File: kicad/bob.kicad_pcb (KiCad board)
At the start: 2 copper layers, 58.4 x 25.4 mm, 54 parts, among them J1 Mini USB Female, J2 GPIO (Optional), J3 GPIO (Optional), J4 Battery Connector, J5 Conn_01x03_Male, SW1 Screw Switch, U1 W25Q64JVSS, U2 AMS1117-3.3, U3 RP2040, U4 QMC5883L, U5 QMI8658C, U6 HP203B, Y1 12MHz

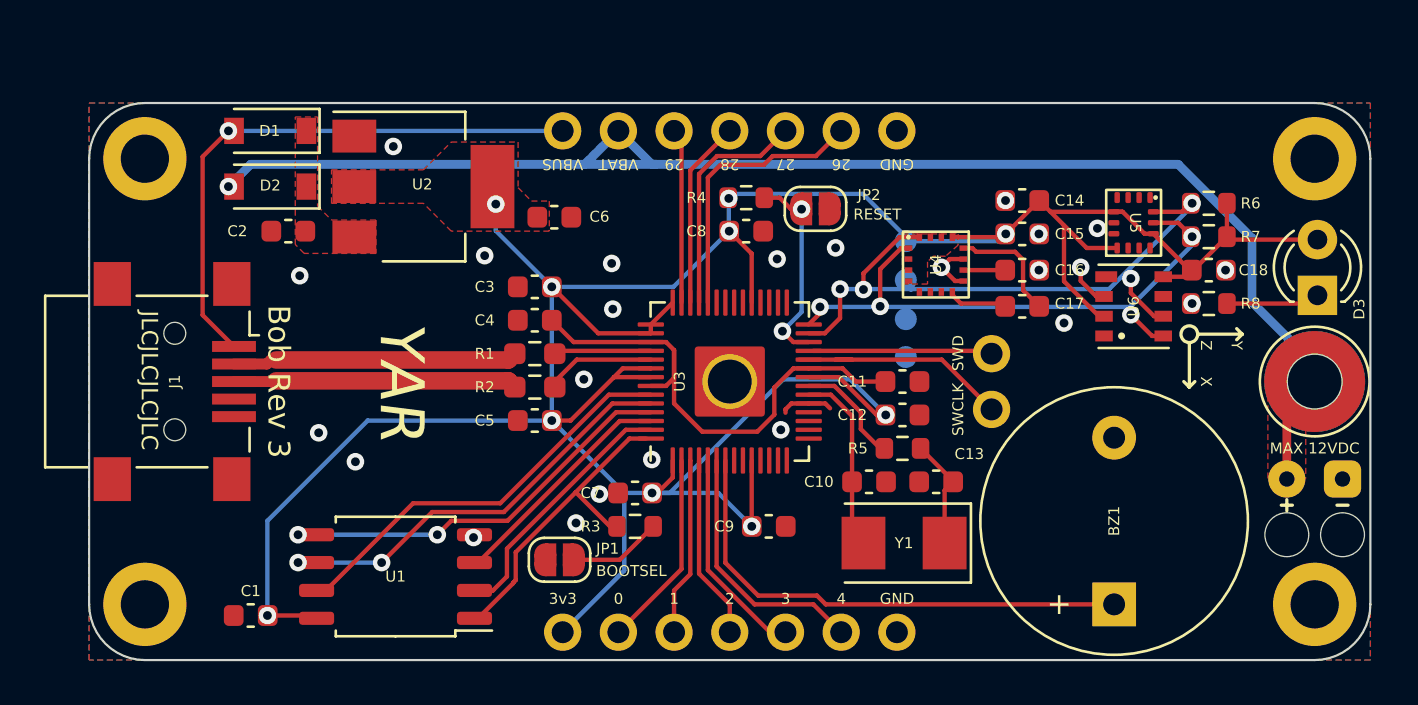
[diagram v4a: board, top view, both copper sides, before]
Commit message: Added pyro channels Added bendy traces Added status LED Removed buzzer
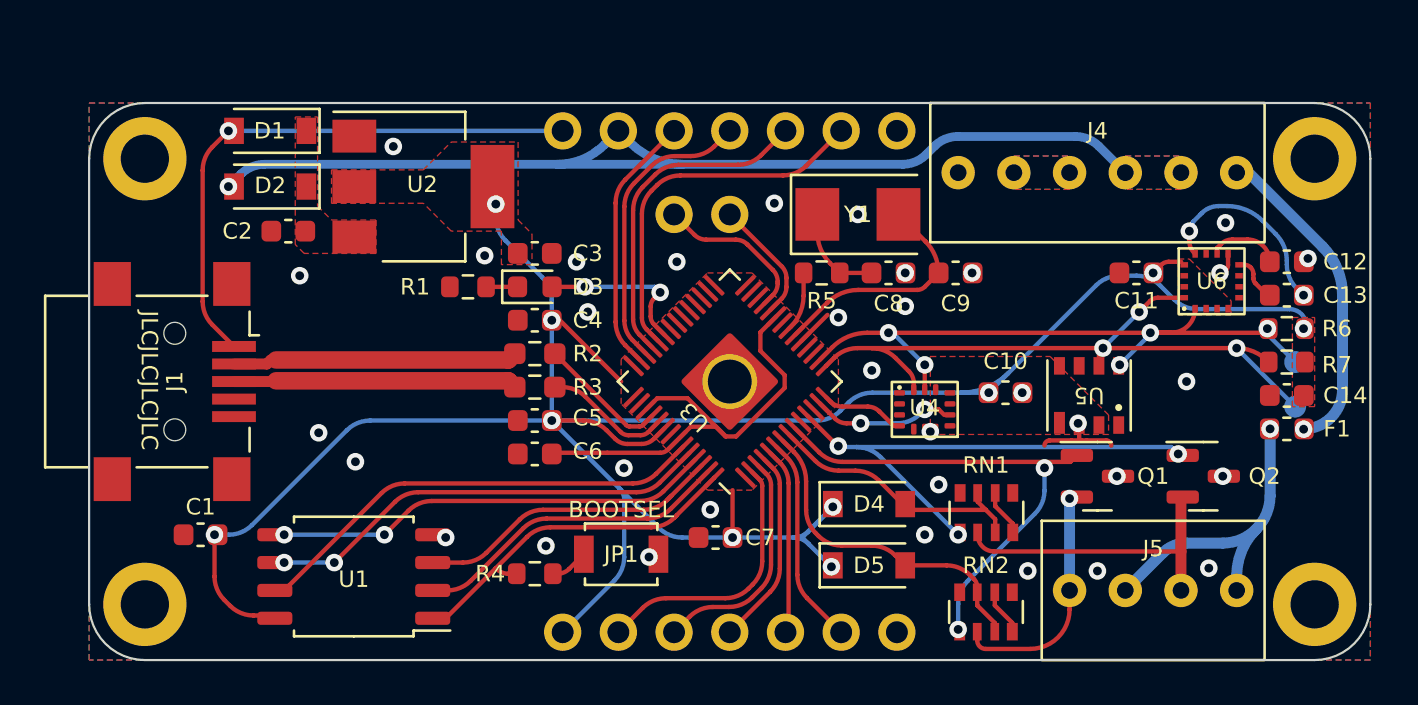
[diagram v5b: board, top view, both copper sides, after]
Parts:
- removed BZ1: Buzzer, Buzzer_Beeper:Buzzer_12x9.5RM7.6
- removed C15, C18: 100n, Capacitor_SMD:C_0603_1608Metric
- removed C16: 4.7u, Capacitor_SMD:C_0603_1608Metric
- removed C17: 220n, Capacitor_SMD:C_0603_1608Metric
- removed the C7 at (38.9, 35.6)
- removed the C8 at (43.9, 23.6)
- removed JP2: RESET, Jumper:SolderJumper-2_P1.3mm_Open_RoundedPad1.0x1.5mm
- removed the R4 at (43.9, 22.1)
- removed R8: 100, Resistor_SMD:R_0603_1608Metric
- removed SW1: Screw Switch, Connector:Screw_Switch_M2
- removed TP3, TP4: TestPoint, TestPoint:TestPoint_Pad_D1.0mm
- added C10: 100n, Capacitor_SMD:C_0603_1608Metric, F.Cu at (55.8, 31.0)
- added C13: 220n, Capacitor_SMD:C_0603_1608Metric, F.Cu at (68.6, 26.5)
- added D4: 1N4007, Diode_SMD:D_SOD-123, F.Cu at (49.5, 36.1)
- added D5: 1N4007, Diode_SMD:D_SOD-123, F.Cu at (49.5, 38.9)
- added F1: Polyfuse, Fuse:Fuse_0603_1608Metric, F.Cu at (68.6, 32.6)
- added J5: Conn_01x04_Male, YAR_Connectors:ScrewTerm_2.54x04, F.Cu at (62.5, 40.0)
- added Q1: IRFML8244TRPBF, Package_TO_SOT_SMD:SOT-23, F.Cu at (59.9, 34.8)
- added Q2: IRFML8244TRPBF, Package_TO_SOT_SMD:SOT-23, F.Cu at (64.8, 34.8)
- added R1: 220, Resistor_SMD:R_0603_1608Metric, F.Cu at (31.2, 26.2)
- added RN1: 22k, Resistor_SMD:R_Array_Convex_4x0603, F.Cu at (54.9, 36.5)
- added RN2: 22k, Resistor_SMD:R_Array_Convex_4x0603, F.Cu at (54.9, 41.0)
- C12: value 100n -> 4.7u
- D3: footprint LED_THT:LED_D3.0mm -> LED_SMD:LED_0603_1608Metric
- J4: value Battery Connector -> Screw Terminal, 2.54mm; footprint Connector_Wire:Compact_Relief -> YAR_Connectors:ScrewTerm_2.54x06; moved to F.Cu
- JP1: footprint Jumper:SolderJumper-2_P1.3mm_Open_RoundedPad1.0x1.5mm -> Button_Switch_SMD:SW_SPST_B3U-1000P
- U3: footprint RP2040_minimal:RP2040-QFN-56_HS -> YAR_MCU:RP2040-QFN-56_HS
- U4: value QMC5883L -> QMI8658C; footprint Silicon-Custom:LGA-16-3X3 -> YAR_Sensors:QMI8658C-LGA14
- U5: value QMI8658C -> HP203B; footprint Silicon-Custom:14LGA_2.5x3.0 -> YAR_Sensors:HP203B-LGA8
- U6: value HP203B -> QMC5883L; footprint RP2040_minimal:LGA-8_3.6x3.8x0.9P -> YAR_Sensors:QMC5883L-LGA16
- YAR: moved to B.Cu
- moved D3 35.7 mm to (34.3, 26.2), turned to 0 degrees
- moved C12 18.9 mm to (68.6, 25.0), turned to 180 degrees
- moved TP2 18.7 mm to (69.0, 31.6), turned to -90 degrees
- moved TP1 18.6 mm to (69.0, 29.6), turned to -90 degrees
- moved J4 17.9 mm to (59.9, 21.0), turned to 0 degrees
- moved J6 15.8 mm to (40.6, 22.9), turned to -90 degrees
- moved Y1 15.1 mm to (49.0, 22.9), turned to 0 degrees
- moved C14 15.0 mm to (68.6, 31.1)
- moved C11 11.8 mm to (61.7, 25.5), turned to 180 degrees
- moved C9 10.3 mm to (53.5, 25.5)
- moved C8 9.77 mm to (50.4, 25.5), turned to 180 degrees
- moved R5 8.81 mm to (47.4, 25.5)
- moved U5 8.13 mm to (59.6, 31.1), turned to 180 degrees
- moved R6 6.73 mm to (68.6, 28.1)
- moved R7 6.73 mm to (68.6, 29.6)
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- renumbered C6 to C3, C3 to C4, C4 to C6, C9 to C7, C13 to C8, C10 to C9, J5 to J6, R1 to R2, R2 to R3, R3 to R4
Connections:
- C11 pad 1: +1V1 -> +3V3
- C12 pad 1: +3V3 -> GND
- C12 pad 2: GND -> Net-(C17-Pad2)
- D3 pad 2: +3V3 -> Net-(D1-Pad2)
- J4 pad 2: Net-(J4-Pad2) -> Net-(J2-Pad2)
- R6 pad 1: I2C_SDA -> I2C_SCL
- R7 pad 1: I2C_SCL -> I2C_SDA
- TP1 pad 1: +3V3 -> I2C_SCL
- U3 pad 11: unconnected-(U3-Pad11) -> Pyro 2
- U3 pad 13: unconnected-(U3-Pad13) -> QMI_INT2
- U3 pad 14: unconnected-(U3-Pad14) -> QMI_INT1
- U3 pad 15: unconnected-(U3-Pad15) -> I2C_SDA
- U3 pad 16: unconnected-(U3-Pad16) -> I2C_SCL
- U3 pad 26: Net-(JP2-Pad2) -> +3V3
- U3 pad 27: I2C_SDA -> unconnected-(U1-Pad27)
- U3 pad 28: I2C_SCL -> unconnected-(U1-Pad28)
- U3 pad 37: unconnected-(U3-Pad37) -> Net-(D1-Pad2)
- U3 pad 7: BUZZER -> Cont 1
- U3 pad 8: unconnected-(U3-Pad8) -> Cont 2
- U3 pad 9: unconnected-(U3-Pad9) -> Pyro 1
- U4 pad 1: I2C_SCL -> GND
- U4 pad 10: Net-(C16-Pad2) -> (no net)
- U4 pad 11: GND -> (no net)
- U4 pad 12: Net-(U4-Pad12) -> +3V3
- U4 pad 13: +3V3 -> I2C_SCL
- U4 pad 14: (no net) -> I2C_SDA
- U4 pad 2: +3V3 -> GND
- U4 pad 3: (no net) -> GND
- U4 pad 4: +3V3 -> QMI_INT1
- U4 pad 6: (no net) -> GND
- U4 pad 7: (no net) -> GND
- U4 pad 8: Net-(C17-Pad1) -> +3V3
- U4 pad 9: GND -> QMI_INT2
- U5 pad 1: GND -> unconnected-(U5-Pad1)
- U5 pad 3: GND -> +3V3
- U5 pad 4: unconnected-(U5-Pad4) -> (no net)
- U5 pad 5: +3V3 -> I2C_SCL
- U5 pad 6: GND -> I2C_SDA
- U5 pad 7: GND -> unconnected-(U5-Pad7)
- U6 pad 1: unconnected-(U6-Pad1) -> I2C_SCL
- U6 pad 2: GND -> +3V3
- U6 pad 3: +3V3 -> (no net)
- U6 pad 4: unconnected-(U6-Pad4) -> +3V3
- U6 pad 5: I2C_SCL -> (no net)
- U6 pad 6: I2C_SDA -> (no net)
- U6 pad 7: unconnected-(U6-Pad7) -> (no net)
- U6 pad 8: +3V3 -> Net-(C18-Pad1)
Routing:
- net +3V3: track 147.0 -> 117.1 mm
- net Pyro 2: track 0.00 -> 24.2 mm, vias 0 -> 3
- net BUZZER: track 23.2 -> 0.00 mm
- net Pyro 1: track 0.00 -> 22.7 mm, vias 0 -> 2
- net Cont 1: track 0.00 -> 15.3 mm
- net ARM: track 0.00 -> 15.1 mm, vias 0 -> 1
- net Net-(F1-Pad1): track 0.00 -> 15.0 mm, vias 0 -> 1
- net Fire 2: track 0.00 -> 14.1 mm
- net Cont 2: track 0.00 -> 12.4 mm
- net Fire 1: track 0.00 -> 10.8 mm, vias 0 -> 1
- net +BATT: track 59.0 -> 48.9 mm
- net Net-(C18-Pad2): track 0.00 -> 9.30 mm, vias 0 -> 2
- net Net-(JP2-Pad2): track 9.22 -> 0.00 mm, vias 2 -> 0
- net Net-(D1-Pad2): track 0.00 -> 7.37 mm, vias 0 -> 2
- net QMI_INT2: track 0.00 -> 6.32 mm, vias 0 -> 2
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- added copper zone on F.Cu, net +BATT
- added copper zone on B.Cu, net Net-(J2-Pad2)
- added copper zone on F.Cu, net Net-(J2-Pad2)
- removed copper zone on F.Cu, net Net-(J4-Pad2)
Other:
- board text added: "+ -"
- board text added: "ARM"
- board text added: "BAT"
- board text added: "BUS"
- board text added: "Bob Rev 4"
- board text added: "CLK"
- board text added: "PYRO 1"
- board text added: "PYRO 2"
- board text added: "SWITCH"
- board text removed: "3v3"
- board text removed: "Bob Rev 3"
- board text removed: "MAX 12VDC"
- board text removed: "RESET"
- board text removed: "SWCLK"
- board text removed: "VBAT"
- board text removed: "VBUS"
- board text removed: "X"
- board text removed: "Y"
- board text removed: "Z"

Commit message: Started work on bob R4
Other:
- board text added: "X"
- board text added: "Y"
- board text added: "Z"
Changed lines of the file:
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@@
       (net 14 "I2C_SDA") (pinfunction "1") (pintype "passive"))
   )
+  (gr_line (start 62.611 33.147) (end 61.849 32.385) (layer "B.SilkS") (width 0.15))
   (gr_line (start 67.564 36.83) (end 67.564 43.18) (layer "B.SilkS") (width 0.15))
   (gr_line (start 67.564 17.78) (end 67.564 24.13) (layer "B.SilkS") (width 0.15))
+  (gr_line (start 66.421 32.766) (end 62.768815 32.766) (layer "B.SilkS") (width 0.15))
   (gr_line (start 62.484 17.78) (end 62.484 24.13) (layer "B.SilkS") (width 0.15))
   (gr_line (start 52.324 17.907) (end 52.324 24.13) (layer "B.SilkS") (width 0.15))
   (gr_line (start 57.404 24.13) (end 57.404 17.653) (layer "B.SilkS") (width 0.15))
   (gr_line (start 57.404 36.83) (end 57.404 43.18) (layer "B.SilkS") (width 0.15))
+  (gr_line (start 62.23 28.575) (end 61.722 29.083) (layer "B.SilkS") (width 0.15))
+  (gr_circle (center 62.23 32.766) (end 62.611 32.385) (layer "B.SilkS") (width 0.15) (fill none))
   (gr_line (start 62.484 36.957) (end 62.484 43.18) (layer "B.SilkS") (width 0.15))
+  (gr_line (start 66.421 32.766) (end 65.913 33.274) (layer "B.SilkS") (width 0.15))
+  (gr_line (start 61.849 33.147) (end 62.611 32.385) (layer "B.SilkS") (width 0.15))
+  (gr_line (start 62.23 28.575) (end 62.23 32.227185) (layer "B.SilkS") (width 0.15))
   (gr_circle (center 69.85 40.64) (end 71 40.64) (layer "Dwgs.User") (width 0.15) (fill none))
   (gr_circle (center 16.51 20.32) (end 17.66 20.32) (layer "Dwgs.User") (width 0.15) (fill none))
@@
     (effects (font (size 0.75 0.75) (thickness 0.15)) (justify mirror))
   )
+  (gr_text "Y" (at 62.738 28.956) (layer "B.SilkS")
+    (effects (font (size 0.75 0.75) (thickness 0.15)) (justify mirror))
+  )
   (gr_text "BAT" (at 38.1 20.574 180) (layer "B.SilkS")
     (effects (font (size 0.75 0.75) (thickness 0.15)) (justify mirror))
   )
   (gr_text "0" (at 38.105 40.386) (layer "B.SilkS")
+    (effects (font (size 0.75 0.75) (thickness 0.15)) (justify mirror))
+  )
+  (gr_text "Z" (at 62.738 31.623) (layer "B.SilkS")
     (effects (font (size 0.75 0.75) (thickness 0.15)) (justify mirror))
   )
@@
     (effects (font (size 0.75 0.75) (thickness 0.15)) (justify mirror))
   )
+  (gr_text "X" (at 66.167 32.131 180) (layer "B.SilkS")
+    (effects (font (size 0.75 0.75) (thickness 0.15)) (justify mirror))
+  )
